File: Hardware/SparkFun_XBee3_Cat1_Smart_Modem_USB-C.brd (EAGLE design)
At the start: 33 x 62.2 mm, 101 parts, among them J4 QWIIC_RIGHT_ANGLE, U2 AP63203, U5 ESD Diode, U6 CP210X

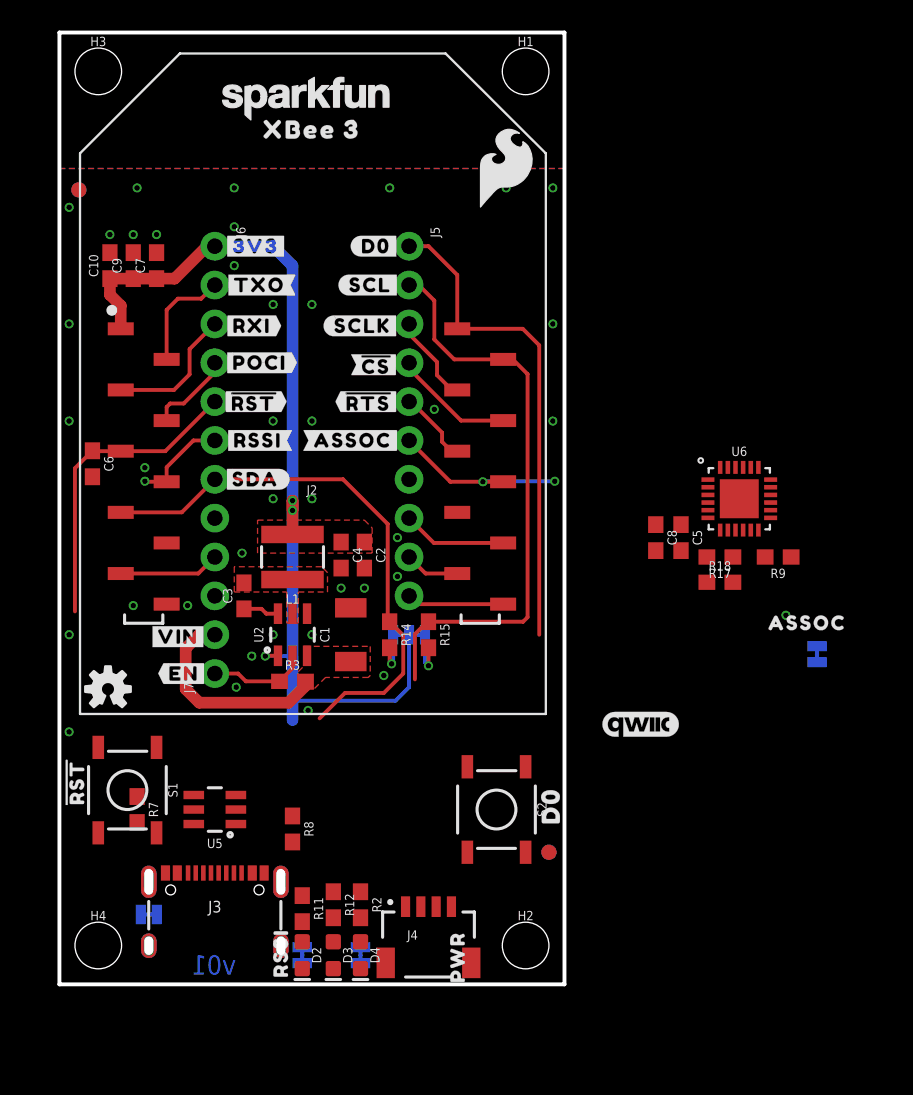
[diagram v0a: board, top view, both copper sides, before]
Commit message: Moves parts around
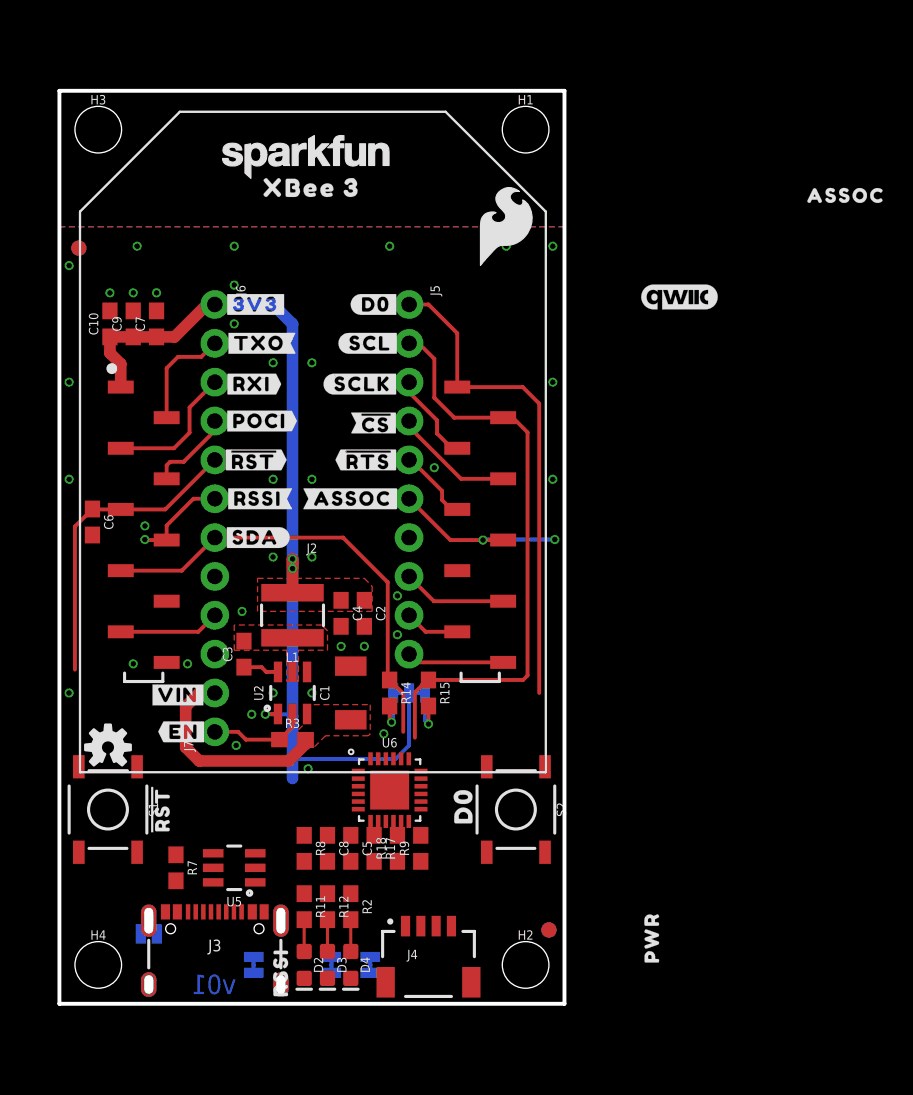
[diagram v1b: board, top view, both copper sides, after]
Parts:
- removed FRAME2: FRAME-LETTER, SparkFun-Aesthetics:CREATIVE_COMMONS
- added FRAME1: FRAME-LEDGER, SparkFun-Aesthetics:CREATIVE_COMMONS
- moved U$52 51.4 mm to (48.1, 40.0)
- moved U$51 38.6 mm to (49.5, 42.8), turned to 270 degrees
- moved ALED 37.7 mm to (17.8, 2.54)
- moved R9 30.1 mm to (23.6, 10.2), turned to 90 degrees
- moved U6 29.8 mm to (21.6, 14.0)
- moved C5 29.6 mm to (19.1, 10.2)
- moved R17 29.6 mm to (20.6, 10.2), turned to 270 degrees
- moved C8 29.6 mm to (17.5, 10.2)
- moved LOGO3 28.1 mm to (40.5, 46.2)
- moved U$43 28.1 mm to (51.4, 52.8)
- moved U$49 28.1 mm to (48.8, 50.8)
- moved R18 27.3 mm to (22.1, 10.2), turned to 90 degrees
- moved U$42 12.8 mm to (38.7, 4.32)
- moved U$30 5.86 mm to (6.60, 12.7)
- moved U$40 5.71 mm to (26.4, 13.0)
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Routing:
- net D11/SDA: track 36.4 -> 29.8 mm
- net N$7: track 0.00 -> 2.08 mm
- net N$2: track 0.00 -> 2.08 mm
- net N$12: track 0.00 -> 2.08 mm
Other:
- board size 33 x 62.2 mm -> 33 x 59.7 mm

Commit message: Routes board
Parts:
- J3: value (none) -> USB Female Type C Connector; device SparkFun-Connectors:USB-C-16P-2LAYER-PADS -> SparkFun-Connectors:USB-C-16P-4LAYER-ISOLATED
- moved U$62 22.1 mm to (36.4, 4.57)
- moved I2C_PU 12.0 mm to (26.7, 8.89)
- moved U$26 12.0 mm to (26.7, 7.24)
- moved R14 12.0 mm to (25.1, 8.89)
- moved R15 11.7 mm to (26.7, 8.89)
- moved ALED 3.69 mm to (21.5, 2.41)
- moved SHLD 3.12 mm to (8.61, 6.02), turned to 270 degrees
- moved D4 3.05 mm to (16.0, 2.54)
- moved R2 3.05 mm to (16.0, 6.35)
- moved C10 3.05 mm to (6.35, 44.5)
- moved C7 3.05 mm to (3.30, 44.5)
- moved PLED 2.67 mm to (15.4, 2.36)
- moved RLED 1.78 mm to (18.5, 2.41)
- moved D2 1.52 mm to (17.5, 2.54)
- moved D3 1.52 mm to (19.1, 2.54)
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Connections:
- net SHLD: now also J3.SHLD5, J3.SHLD6, J3.SHLD7, J3.SHLD8
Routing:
- net 3.3V: track 63.6 -> 25.6 mm, vias 3 -> 8
- net D13/TXO: track 7.06 -> 42.0 mm
- net D10/RSSI_PWM: track 6.26 -> 39.2 mm, vias 1 -> 2
- net D14/RXI: track 8.91 -> 41.7 mm
- net D5/ASSOCIATE: track 12.0 -> 41.9 mm
- net D8/!DTR!: track 6.60 -> 31.1 mm
- net D11/SDA: track 29.8 -> 54.1 mm, vias 0 -> 2
- net D6/!RTS!: track 4.84 -> 26.2 mm, vias 0 -> 2
- net D+: track 0.04 -> 20.3 mm, vias 0 -> 2
- net D-: track 0.00 -> 18.0 mm
- net !RESET!: track 20.3 -> 35.1 mm
- net VIN: track 13.9 -> 25.4 mm, vias 0 -> 2
- net D0: track 32.2 -> 42.7 mm
- net D1/SCL: track 38.4 -> 47.7 mm
- net N$5: track 0.00 -> 5.96 mm
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- added copper zone on layer 15, net 3.3V
- added copper zone on layer 2, net GND
- added copper zone on layer 1, net SHLD
- added copper zone on layer 16, net SHLD
- added copper zone on layer 1, net V_USB

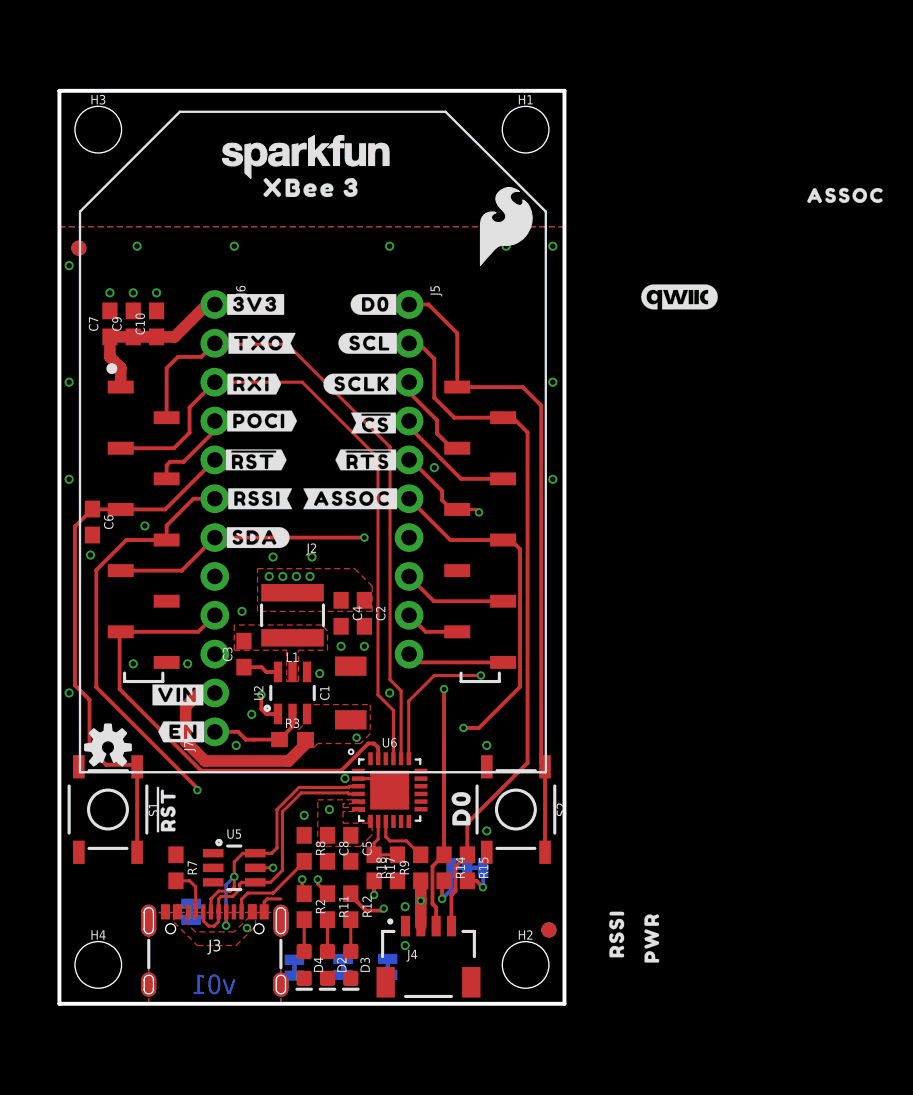
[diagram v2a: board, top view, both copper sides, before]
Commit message: Commits (finally) to shrinking the LED resistors so that I can fit in labels
* Increases schematic frame size to Ledger
* Adds measures
* Adds additional silk
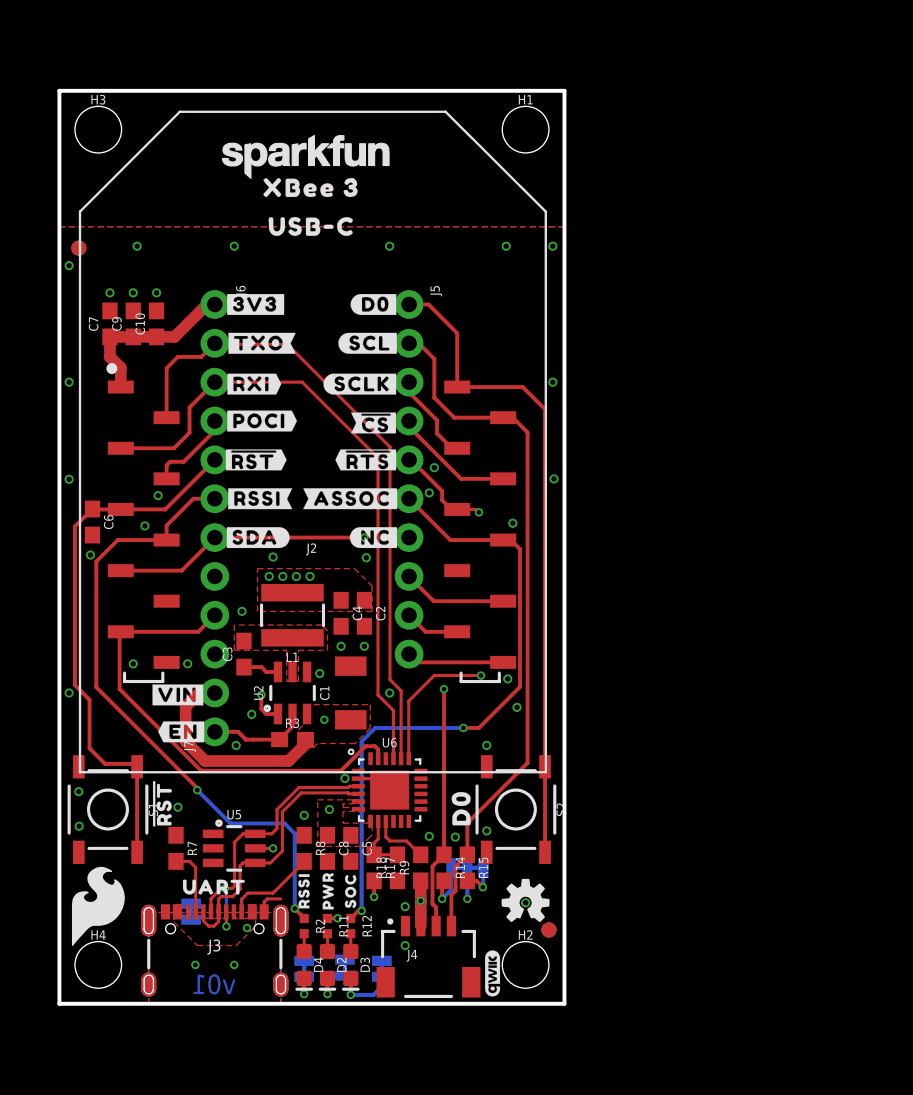
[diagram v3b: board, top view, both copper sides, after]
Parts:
- removed U$42: (no value), top:PWR26
- removed U$43: (no value), top:ASSOC27
- removed U$62: (no value), top:RSSI31
- added U$1: (no value), topmirror:RSSI31
- added U$10, U$7: (no value), botmirror:#NC#3
- added U$2: (no value), topmirror:PWR29
- added U$24, U$25: (no value), topmirror:USB#C1342
- added U$28: (no value), topmirror:UART34
- added U$3: (no value), topmirror:SOC30
- added U$4: (no value), topmirror:#SHLD#36
- added U$5: (no value), topmirror:#NC#1
- LOGO3: value QWIIC_LOGO_5MM -> QWIIC_LOGO_3MM; device SparkFun-Aesthetics:QWIIC_5MM -> SparkFun-Aesthetics:QWIIC_3MM
- R11, R12, R2: device SparkFun-Resistors:0603 -> SparkFun-Resistors:0402-TIGHT
- moved U$49 52.8 mm to (21.1, 5.84), turned to 90 degrees
- moved U$61 51.8 mm to (2.54, 6.35)
- moved U$51 49.9 mm to (16.0, 5.84), turned to 90 degrees
- moved LOGO3 45.9 mm to (28.3, 1.98), turned to 90 degrees
- moved U$52 45.1 mm to (18.7, 5.84), turned to 90 degrees
- moved LOGO2 29.1 mm to (30.5, 6.60)
- moved PLED 3.30 mm to (18.7, 2.36)
- moved RLED 2.54 mm to (16.0, 2.29)
- moved R11 1.27 mm to (17.5, 5.08)
- moved R12 1.27 mm to (19.1, 5.08)
- moved R2 1.27 mm to (16.0, 5.08)
- moved R7 1.27 mm to (7.62, 10.2)
- moved U5 1.27 mm to (11.4, 10.2)
- moved U$30 0.46 mm to (6.73, 13.1)
- moved ALED 0.40 mm to (21.1, 2.29)
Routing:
- net D5/ASSOCIATE: track 41.9 -> 58.2 mm
- net D10/RSSI_PWM: track 39.2 -> 53.1 mm
- net VIN: track 25.4 -> 29.3 mm
- net N$21: track 0.18 -> 3.97 mm, vias 0 -> 1
- net N$23: track 0.00 -> 3.23 mm, vias 0 -> 1
- net N$3: track 0.00 -> 2.16 mm, vias 0 -> 1
- net D1/SCL: track 47.7 -> 46.0 mm
- net 3.3V: track 25.6 -> 27.1 mm, vias 8 -> 9
- net N$6: track 3.09 -> 4.36 mm
- net V_USB: track 5.81 -> 7.08 mm
- net N$7: track 2.08 -> 1.16 mm
- net N$2: track 2.08 -> 1.16 mm
- net N$12: track 2.08 -> 1.16 mm
- net D+: track 20.3 -> 19.5 mm
- net GND: vias 34 -> 45

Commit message: Replaces UART IC
* Cuts back ground pour to make room for smaller modules RF singnals
* Fixes polygons
* Adds yellow LED
* Adds additional decoupling caps for RF board
* Increases the size of the board by 0.1" to make space for decoupling caps
* Updates the inductor for switching regulator
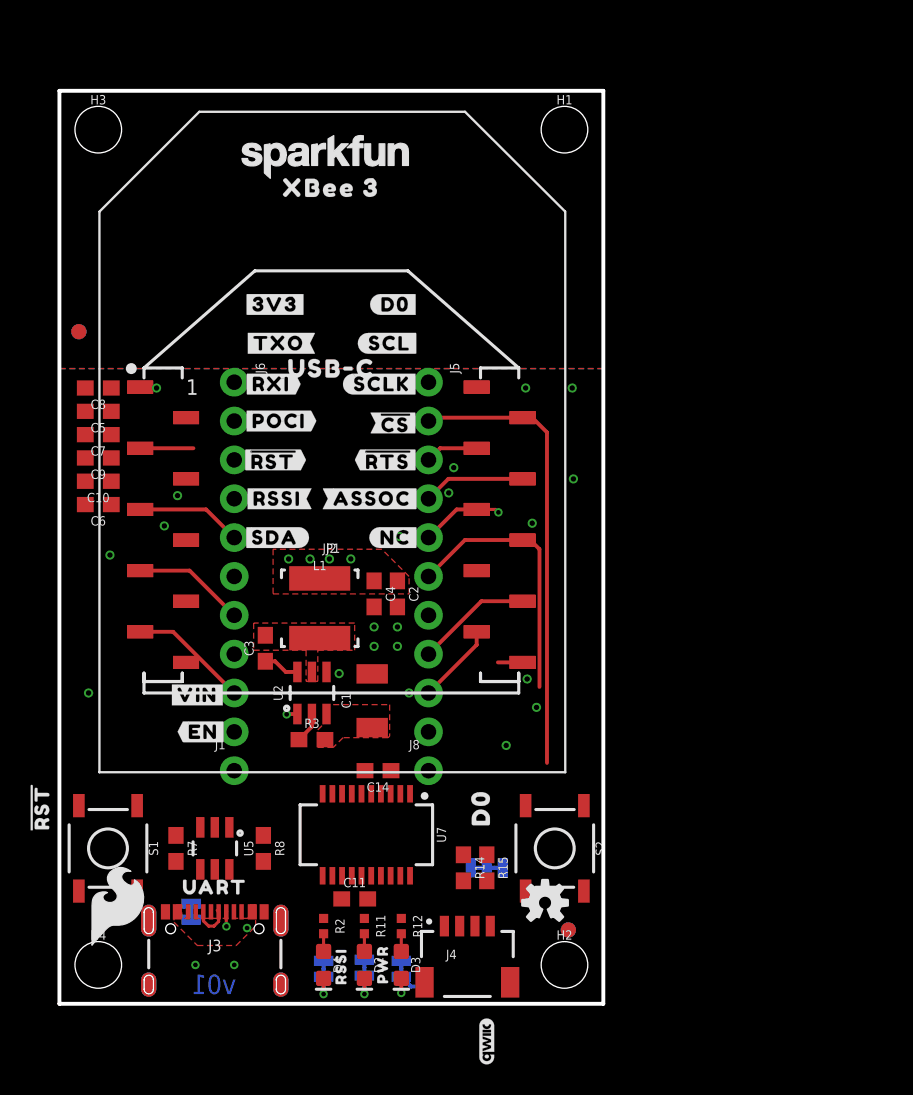
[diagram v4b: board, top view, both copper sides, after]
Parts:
- removed J7: (no value), SparkFun-Connectors:1X02_NO_SILK
- removed R17: 22k, SparkFun-Resistors:0603
- removed R18: 33k, SparkFun-Resistors:0603
- removed R9: 10k, SparkFun-Resistors:0603
- removed U$3: (no value), topmirror:SOC30
- removed U6: CP210X, SparkFun-IC-Comms:QFN24
- added C11, C14: 0.1uF, SparkFun-Capacitors:0603
- added J1, J8: (no value), SparkFun-Connectors:1X01_NO_SILK_STAND
- added JP1: (no value), SparkFun-RF:XBEE-SMD
- added U7: FT231XS, SparkFun-IC-Comms:SSOP20_L
- C5: value 0.1uF -> 47pF
- C8: value 4.7uF -> 10pF
- D2: value RED -> Red
- D4: value BLUE -> Yellow
- L1: value 4.7μH -> 3.9UH; device SparkFun-Coils:INDUCTOR_4X4MM -> SparkFun-Coils:INDUCTOR_3.9UH
- R11: value 1k -> 4.7k
- moved C8 33.6 mm to (2.54, 40.3), turned to 180 degrees
- moved C5 33.0 mm to (2.54, 38.7), turned to 180 degrees
- moved C10 11.0 mm to (2.54, 34.2), turned to 180 degrees
- moved U$53 9.36 mm to (17.8, 40.3)
- moved U$24 9.36 mm to (17.8, 41.5)
- moved C9 9.06 mm to (2.54, 35.7), turned to 180 degrees
- moved U$30 8.01 mm to (-1.27, 12.8)
- moved C7 7.28 mm to (2.54, 37.2), turned to 180 degrees
- moved U$2 5.99 mm to (21.1, 2.57)
- moved U$1 5.51 mm to (18.4, 2.44)
- moved FD1 5.46 mm to (1.27, 43.9)
- moved FD2 5.46 mm to (1.27, 43.9)
- moved J5 5.24 mm to (24.1, 40.6)
- moved J6 5.24 mm to (11.4, 40.6)
- moved LOGO3 4.46 mm to (27.9, -2.46)
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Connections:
- removed net N$10: R17.1, R18.2, U6.8
- removed net N$4: J2.8
- removed net N$9: R9.2, U6.9
- new net VDD: JP1.1
- net 3.3V: now also C11.1, C14.1, U7.13, U7.14, U7.15, U7.3; no longer R9.1, U6.5, U6.6, U6.7
- net D+: now also U7.11; no longer U6.3
- net D-: now also U7.12; no longer U6.4
- net D13/TXO: now also U7.4; no longer U6.20
- net D14/RXI: now also U7.20; no longer U6.21
- net D6/!RTS!: now also U7.2; no longer U6.19
- net D7/!CTS!: now also U7.9
- net D8/!DTR!: now also U7.1; no longer U6.23
- net EN: now also J8.1; no longer J7.1
- net GND: now also C11.2, C14.2, JP1.10, U7.16, U7.6; no longer R18.1, U6.2, U6.PAD
- net VIN: now also J1.1; no longer J7.2, R17.2
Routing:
- net D10/RSSI_PWM: track 53.1 -> 0.80 mm, vias 2 -> 0
- net D11/SDA: track 54.1 -> 7.36 mm, vias 2 -> 0
- net D0: track 42.7 -> 0.00 mm
- net D13/TXO: track 42.0 -> 0.00 mm
- net D5/ASSOCIATE: track 58.2 -> 17.5 mm, vias 2 -> 0
- net D14/RXI: track 41.7 -> 3.48 mm
- net VIN: track 29.3 -> 0.00 mm, vias 2 -> 0
- net !RESET!: track 35.1 -> 6.91 mm
- net D8/!DTR!: track 30.8 -> 7.91 mm
- net D+: track 19.5 -> 1.00 mm, vias 2 -> 1
- net D1/SCL: track 46.0 -> 29.8 mm
- net 3.3V: track 27.1 -> 10.9 mm, vias 9 -> 5
- net D-: track 17.9 -> 2.64 mm
- net D6/!RTS!: track 26.2 -> 16.1 mm, vias 2 -> 1
- net V_USB: track 7.08 -> 0.25 mm, vias 2 -> 1
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- removed copper zone on layer 1, net SHLD
- removed copper zone on layer 16, net SHLD
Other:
- board size 33 x 59.7 mm -> 35.6 x 59.7 mm

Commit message: Routes some airwires
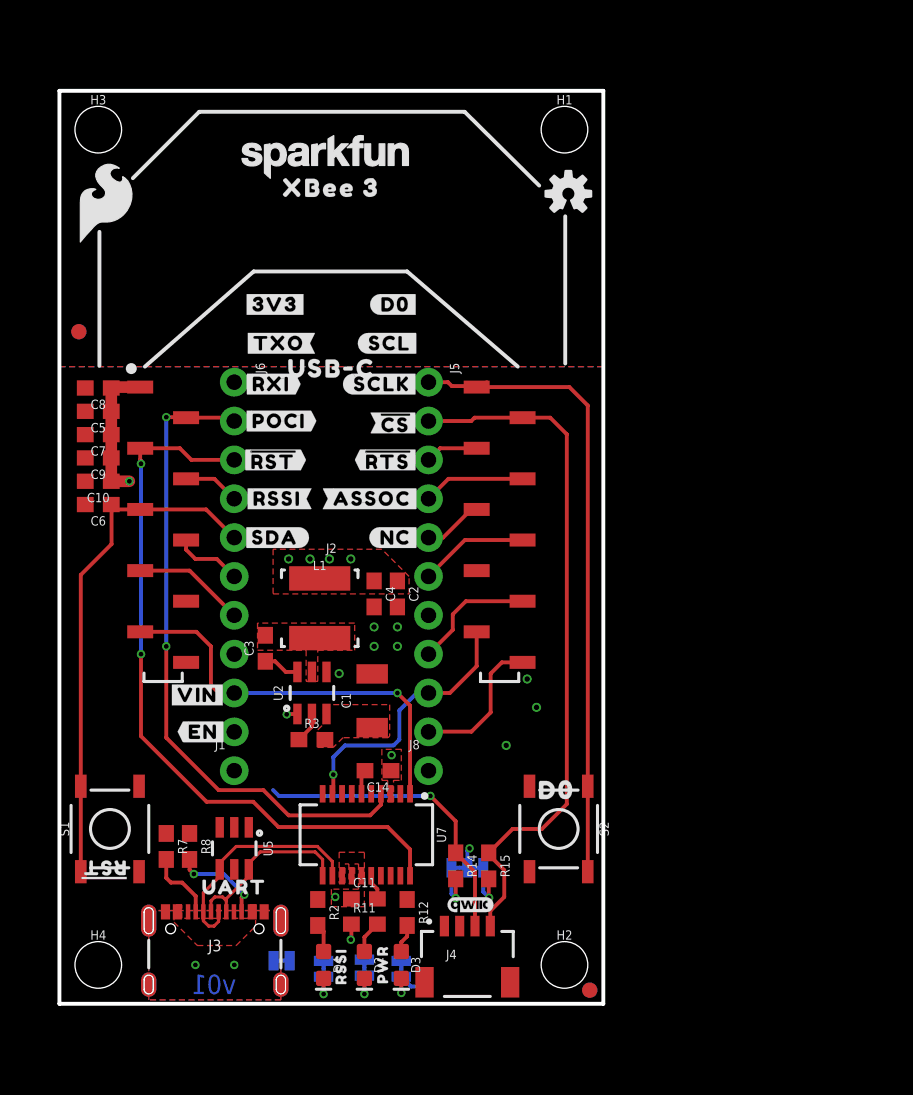
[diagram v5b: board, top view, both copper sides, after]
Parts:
- removed JP1: (no value), SparkFun-RF:XBEE-SMD
- J2: device xbee_smart_modem:XBEE3-SMD_SILK -> xbee_smart_modem:XBEE3-SMD
- R11, R12, R2: device SparkFun-Resistors:0402-TIGHT -> SparkFun-Resistors:0603
- moved LOGO2 46.4 mm to (33.3, 53.0)
- moved U$61 46.0 mm to (3.05, 52.3)
- moved LOGO3 9.00 mm to (26.9, 6.48), turned to 0 degrees
- moved SHLD 6.73 mm to (14.5, 2.82), turned to 0 degrees
- moved U$30 5.84 mm to (2.92, 8.76), turned to 180 degrees
- moved U$40 5.08 mm to (32.5, 14.0), turned to 0 degrees
- moved R8 4.83 mm to (8.51, 10.3)
- moved FD3 4.18 mm to (34.7, 0.89)
- moved FD4 4.18 mm to (34.7, 0.89)
- moved S2 1.30 mm to (32.6, 11.4)
- moved S1 1.28 mm to (3.30, 11.4), turned to 90 degrees
- moved I2C_PU 1.27 mm to (26.7, 8.89)
- moved U$26 1.27 mm to (26.7, 7.24)
- moved U$28 1.27 mm to (11.4, 7.62)
- moved U$52 1.27 mm to (21.2, 5.84)
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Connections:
- removed net VDD: JP1.1
- net GND: no longer JP1.10
- net VIN: no longer C1.1, R3.2, U2.3
- net V_USB: now also C1.1, R3.2, U2.3
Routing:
- net D14/RXI: track 3.48 -> 47.7 mm, vias 0 -> 2
- net D13/TXO: track 0.00 -> 42.6 mm, vias 0 -> 2
- net D0: track 0.00 -> 42.3 mm
- net !RESET!: track 6.91 -> 33.8 mm
- net D11/SDA: track 7.36 -> 27.5 mm, vias 0 -> 1
- net D8/!DTR!: track 7.91 -> 27.0 mm, vias 0 -> 1
- net D1/SCL: track 29.8 -> 46.4 mm
- net D-: track 2.64 -> 15.4 mm
- net D7/!CTS!: track 5.30 -> 17.6 mm, vias 0 -> 1
- net D6/!RTS!: track 16.1 -> 3.91 mm, vias 1 -> 0
- net D+: track 1.00 -> 12.6 mm, vias 1 -> 0
- net 3.3V: track 10.9 -> 22.5 mm, vias 5 -> 10
- net D5/ASSOCIATE: track 17.5 -> 7.64 mm
- net D4/SPI_PICO: track 1.61 -> 9.52 mm
- net N$5: track 0.00 -> 6.13 mm, vias 0 -> 2
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- added copper zone on layer 1, net SHLD
- added copper zone on layer 15, net SHLD
- added copper zone on layer 16, net SHLD
- added copper zone on layer 2, net SHLD
